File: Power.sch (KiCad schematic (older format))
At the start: 40 parts

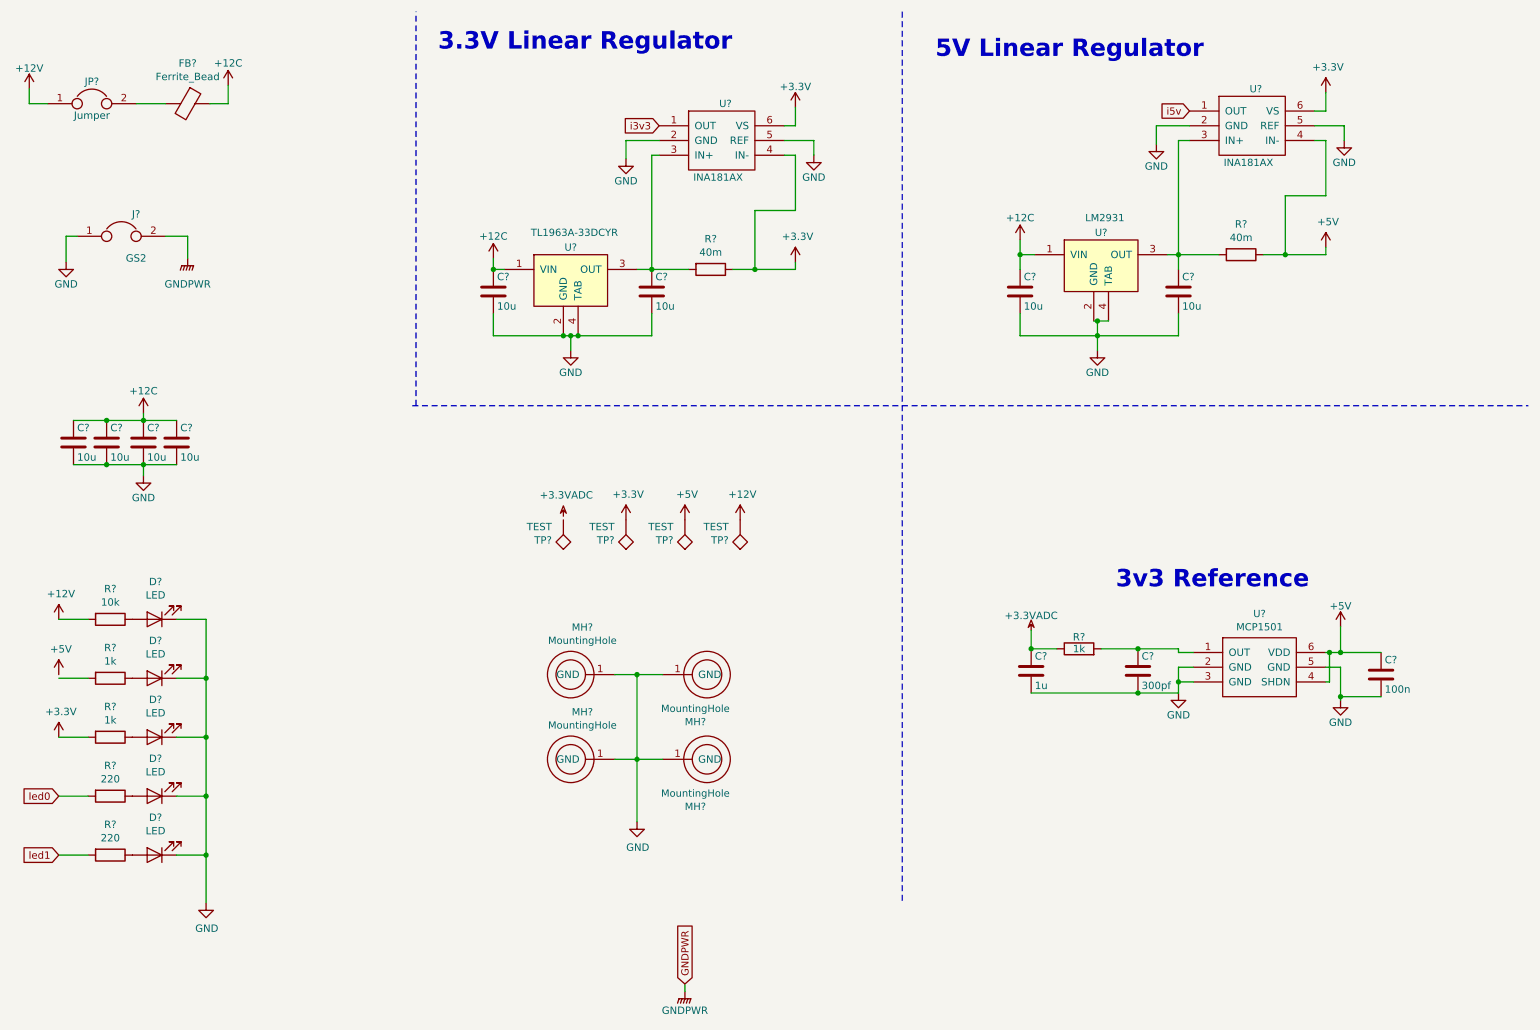
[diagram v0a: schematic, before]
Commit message: Eletrical Rules Check
Fixed some label names
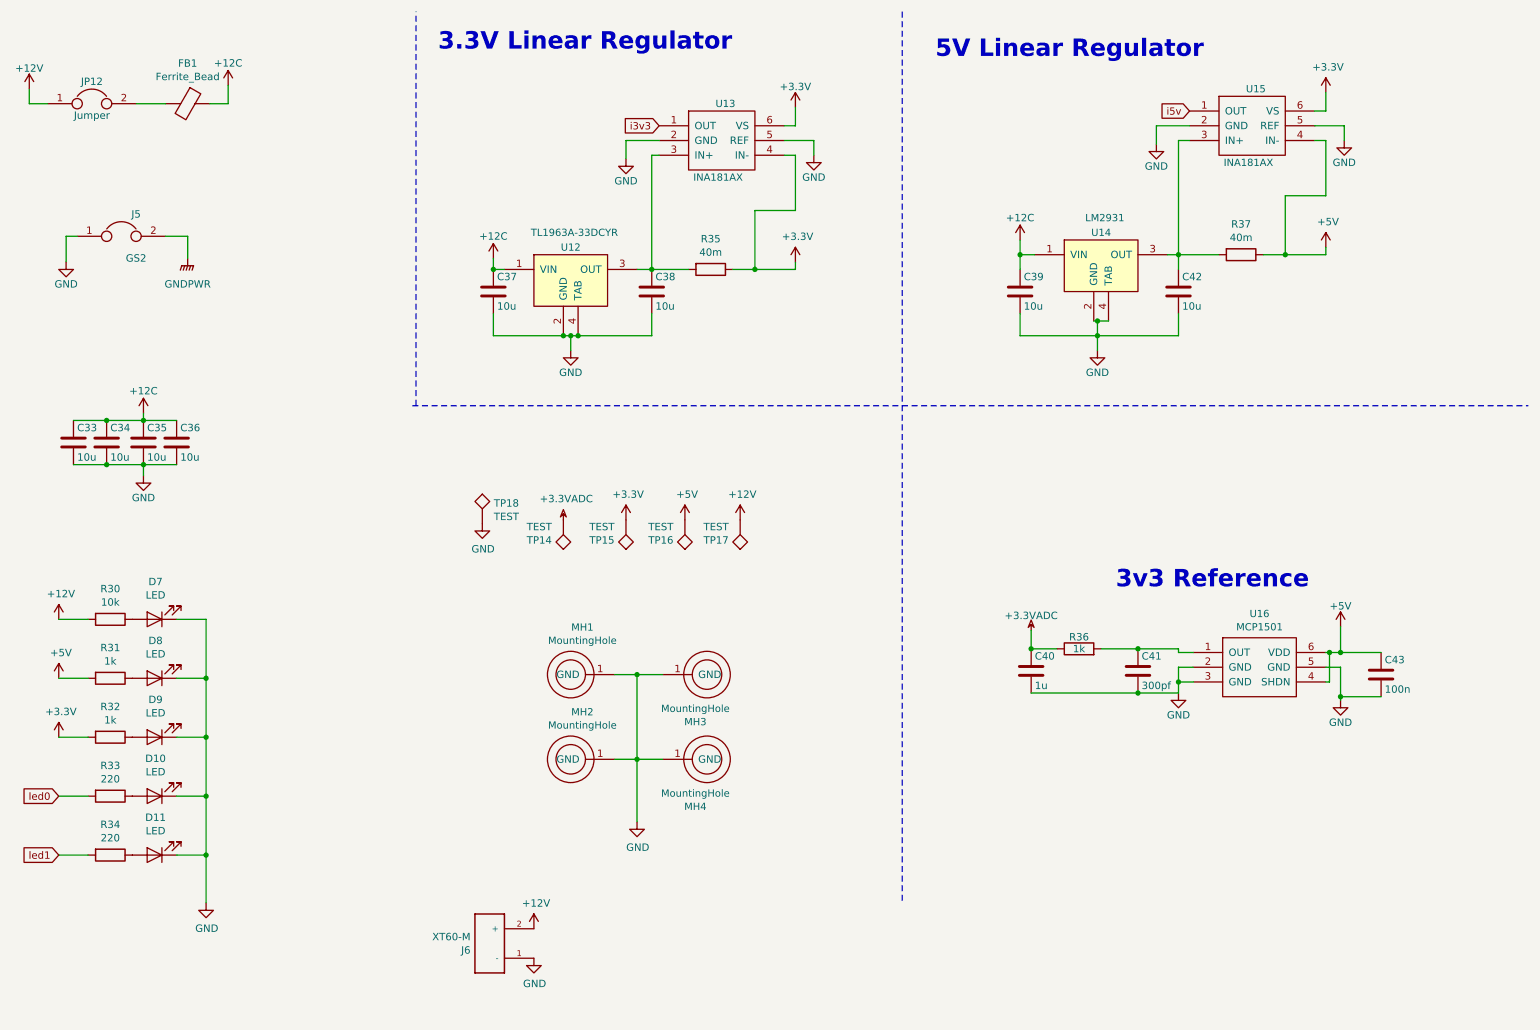
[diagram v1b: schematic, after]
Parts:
- added J6: XT60-M, AMASS_XT60-M, symbol xt60:XT60-M
- added TP18: TEST, symbol ec_2b_rescue:TEST
- gave numbers to parts that had none: 40
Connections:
- net +12V: now also J6.2 (+)
- net +3.3VADC: now also TP14.1
- net +5V: now also R31.2
- net GND: now also J6.1 (-), TP18.1

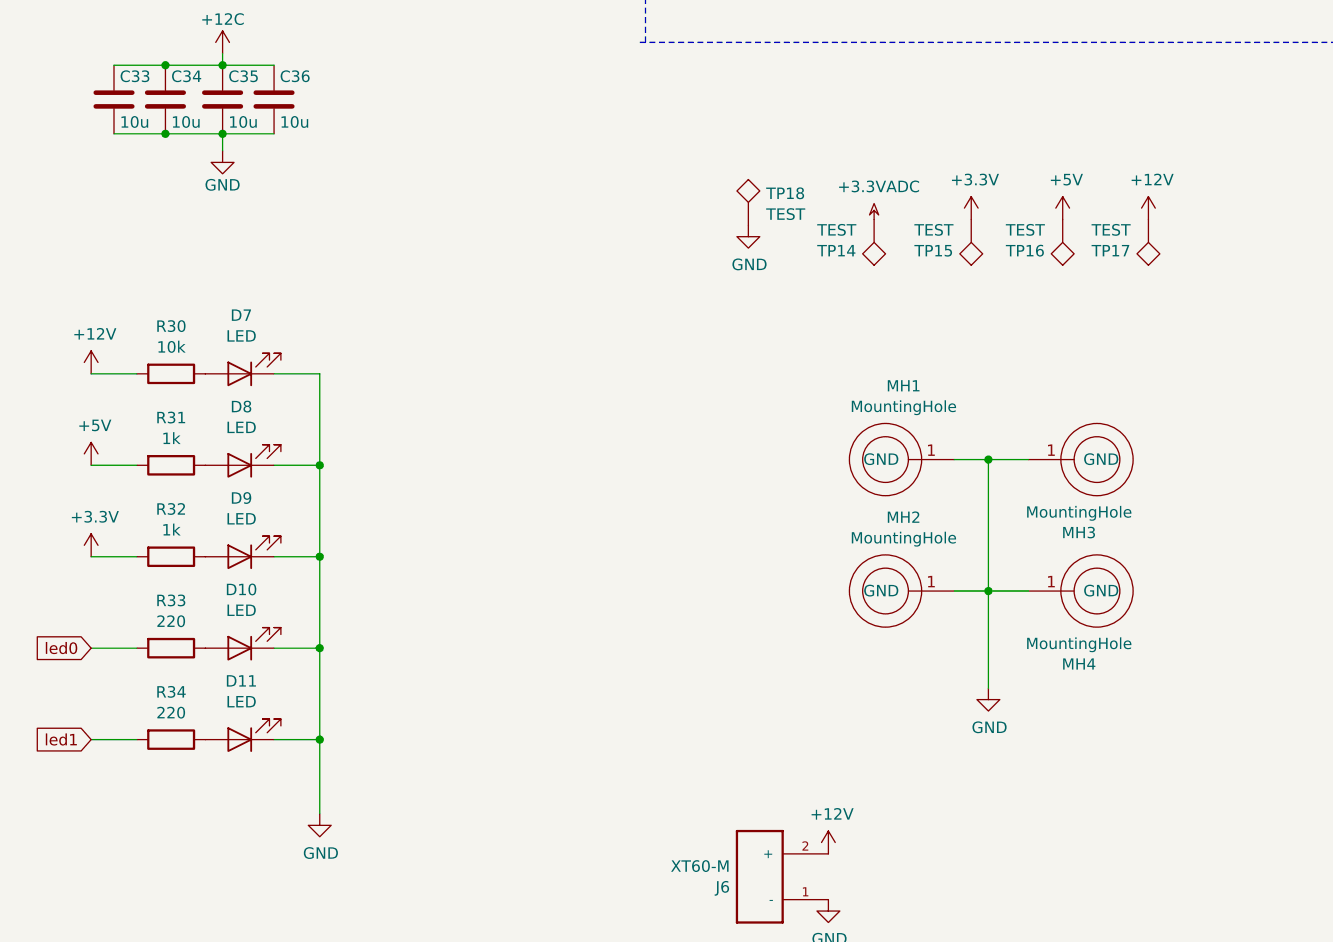
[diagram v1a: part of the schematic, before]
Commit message: Formatting Changes
Made some minor formatting changes. Documented motor channels. Fixed in labels of motor channel.
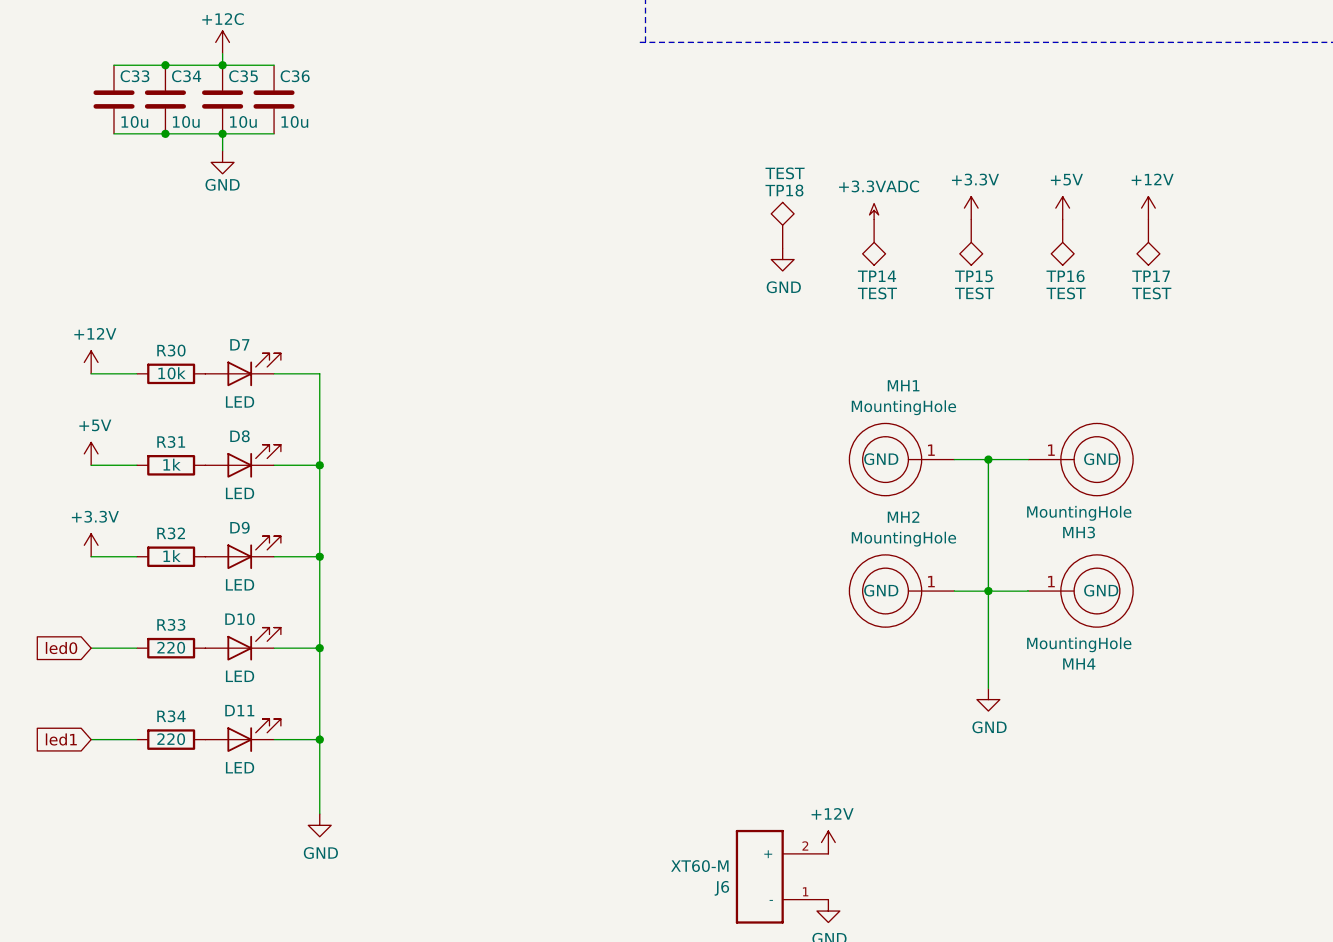
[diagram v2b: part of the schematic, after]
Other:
- moved on the sheet: TP18
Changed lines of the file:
@@
 $Descr A4 11693 8268
 encoding utf-8
-Sheet 12 12
+Sheet 9 12
 Title "Engine Controller Series 3"
 Date ""
@@
 U 1 1 5E6998D2
 P 5875 3925
-F 0 "TP17" H 5953 4063 50  0000 L CNN
-F 1 "TEST" H 5953 3972 50  0000 L CNN
+F 0 "TP17" H 5775 4175 50  0000 L CNN
+F 1 "TEST" H 5775 4250 50  0000 L CNN
 F 2 "" H 5875 3925 50  0001 C CNN
 F 3 "" H 5875 3925 50  0001 C CNN
@@
 U 1 1 5E69A32A
 P 5500 3925
-F 0 "TP16" H 5578 4063 50  0000 L CNN
-F 1 "TEST" H 5578 3972 50  0000 L CNN
+F 0 "TP16" H 5400 4175 50  0000 L CNN
+F 1 "TEST" H 5400 4250 50  0000 L CNN
 F 2 "" H 5500 3925 50  0001 C CNN
 F 3 "" H 5500 3925 50  0001 C CNN
@@
 U 1 1 5E69BC8C
 P 5100 3925
-F 0 "TP15" H 5178 4063 50  0000 L CNN
-F 1 "TEST" H 5178 3972 50  0000 L CNN
+F 0 "TP15" H 5000 4175 50  0000 L CNN
+F 1 "TEST" H 5000 4250 50  0000 L CNN
 F 2 "" H 5100 3925 50  0001 C CNN
 F 3 "" H 5100 3925 50  0001 C CNN
@@
 $EndComp
 $Comp
-L Device:LED D7
-U 1 1 5E6F3842
-P 1900 4600
-F 0 "D7" H 1893 4345 50  0000 C CNN
-F 1 "LED" H 1893 4436 50  0000 C CNN
-F 2 "" H 1900 4600 50  0001 C CNN
-F 3 "~" H 1900 4600 50  0001 C CNN
-	1    1900 4600
-	-1   0    0    1
-$EndComp
-$Comp
-L Device:LED D8
-U 1 1 5E6F68A1
-P 1900 5000
-F 0 "D8" H 1893 4745 50  0000 C CNN
-F 1 "LED" H 1893 4836 50  0000 C CNN
-F 2 "" H 1900 5000 50  0001 C CNN
-F 3 "~" H 1900 5000 50  0001 C CNN
-	1    1900 5000
-	-1   0    0    1
-$EndComp
-$Comp
-L Device:LED D9
-U 1 1 5E6F8653
-P 1900 5400
-F 0 "D9" H 1893 5145 50  0000 C CNN
-F 1 "LED" H 1893 5236 50  0000 C CNN
-F 2 "" H 1900 5400 50  0001 C CNN
-F 3 "~" H 1900 5400 50  0001 C CNN
-	1    1900 5400
-	-1   0    0    1
-$EndComp
-$Comp
-L Device:LED D10
-U 1 1 5E6FA391
-P 1900 5800
-F 0 "D10" H 1893 5545 50  0000 C CNN
-F 1 "LED" H 1893 5636 50  0000 C CNN
-F 2 "" H 1900 5800 50  0001 C CNN
-F 3 "~" H 1900 5800 50  0001 C CNN
-	1    1900 5800
-	-1   0    0    1
-$EndComp
-$Comp
 L Device:LED D11
 U 1 1 5E6FC143
 P 1900 6200
-F 0 "D11" H 1893 5945 50  0000 C CNN
-F 1 "LED" H 1893 6036 50  0000 C CNN
+F 0 "D11" H 1900 6075 50  0000 C CNN
+F 1 "LED" H 1900 6325 50  0000 C CNN
 F 2 "" H 1900 6200 50  0001 C CNN
 F 3 "~" H 1900 6200 50  0001 C CNN
@@
 U 1 1 5E65BE5F
 P 4675 3925
-F 0 "TP14" H 4753 4063 50  0000 L CNN
-F 1 "TEST" H 4753 3972 50  0000 L CNN
+F 0 "TP14" H 4575 4175 50  0000 L CNN
+F 1 "TEST" H 4575 4250 50  0000 L CNN
 F 2 "" H 4675 3925 50  0001 C CNN
 F 3 "" H 4675 3925 50  0001 C CNN
@@
 U 1 1 5E67F268
 P 1600 5000
-F 0 "R31" V 1393 5000 50  0000 C CNN
-F 1 "1k" V 1484 5000 50  0000 C CNN
+F 0 "R31" V 1500 5000 50  0000 C CNN
+F 1 "1k" V 1600 5000 50  0000 C CNN
 F 2 "" V 1530 5000 50  0001 C CNN
 F 3 "~" H 1600 5000 50  0001 C CNN
@@
 U 1 1 5E682C58
 P 1600 5400
-F 0 "R32" V 1393 5400 50  0000 C CNN
-F 1 "1k" V 1484 5400 50  0000 C CNN
+F 0 "R32" V 1500 5400 50  0000 C CNN
+F 1 "1k" V 1600 5400 50  0000 C CNN
 F 2 "" V 1530 5400 50  0001 C CNN
 F 3 "~" H 1600 5400 50  0001 C CNN
@@
 U 1 1 5E68682B
 P 1600 5800
-F 0 "R33" V 1393 5800 50  0000 C CNN
-F 1 "220" V 1484 5800 50  0000 C CNN
+F 0 "R33" V 1500 5800 50  0000 C CNN
+F 1 "220" V 1600 5800 50  0000 C CNN
 F 2 "" V 1530 5800 50  0001 C CNN
 F 3 "~" H 1600 5800 50  0001 C CNN
@@
 U 1 1 5E68A3FE
 P 1600 6200
-F 0 "R34" V 1393 6200 50  0000 C CNN
-F 1 "220" V 1484 6200 50  0000 C CNN
+F 0 "R34" V 1500 6200 50  0000 C CNN
+F 1 "220" V 1600 6200 50  0000 C CNN
 F 2 "" V 1530 6200 50  0001 C CNN
 F 3 "~" H 1600 6200 50  0001 C CNN
@@
 U 1 1 5E678387
 P 1600 4600
-F 0 "R30" V 1393 4600 50  0000 C CNN
-F 1 "10k" V 1484 4600 50  0000 C CNN
+F 0 "R30" V 1500 4600 50  0000 C CNN
+F 1 "10k" V 1600 4600 50  0000 C CNN
 F 2 "" V 1530 4600 50  0001 C CNN
 F 3 "~" H 1600 4600 50  0001 C CNN
@@
 L ec_2b_rescue:TEST TP18
 U 1 1 5E667DA6
-P 4125 3950
-F 0 "TP18" H 4203 4088 50  0000 L CNN
-F 1 "TEST" H 4203 3997 50  0000 L CNN
-F 2 "" H 4125 3950 50  0001 C CNN
-F 3 "" H 4125 3950 50  0001 C CNN
-	1    4125 3950
+P 4275 4050
+F 0 "TP18" H 4200 4300 50  0000 L CNN
+F 1 "TEST" H 4200 4375 50  0000 L CNN
+F 2 "" H 4275 4050 50  0001 C CNN
+F 3 "" H 4275 4050 50  0001 C CNN
+	1    4275 4050
 	1    0    0    -1
 $EndComp
@@
 L ec_2b_rescue:GND #PWR0104
 U 1 1 5E66C108
-P 4125 3950
-F 0 "#PWR0104" H 4125 3700 50  0001 C CNN
-F 1 "GND" H 4130 3777 50  0000 C CNN
-F 2 "" H 4125 3950 50  0001 C CNN
-F 3 "" H 4125 3950 50  0001 C CNN
-	1    4125 3950
+P 4275 4050
+F 0 "#PWR0104" H 4275 3800 50  0001 C CNN
+F 1 "GND" H 4280 3877 50  0000 C CNN
+F 2 "" H 4275 4050 50  0001 C CNN
+F 3 "" H 4275 4050 50  0001 C CNN
+	1    4275 4050
 	1    0    0    -1
 $EndComp
@@
 	1    0    0    -1
 $EndComp
+$Comp
+L Device:LED D10
+U 1 1 5E7D1BBA
+P 1900 5800
+F 0 "D10" H 1900 5675 50  0000 C CNN
+F 1 "LED" H 1900 5925 50  0000 C CNN
+F 2 "" H 1900 5800 50  0001 C CNN
+F 3 "~" H 1900 5800 50  0001 C CNN
+	1    1900 5800
+	-1   0    0    1
+$EndComp
+$Comp
+L Device:LED D9
+U 1 1 5E7D592D
+P 1900 5400
+F 0 "D9" H 1900 5275 50  0000 C CNN
+F 1 "LED" H 1900 5525 50  0000 C CNN
+F 2 "" H 1900 5400 50  0001 C CNN
+F 3 "~" H 1900 5400 50  0001 C CNN
+	1    1900 5400
+	-1   0    0    1
+$EndComp
+$Comp
+L Device:LED D8
+U 1 1 5E7D93E8
+P 1900 5000
+F 0 "D8" H 1900 4875 50  0000 C CNN
+F 1 "LED" H 1900 5125 50  0000 C CNN
+F 2 "" H 1900 5000 50  0001 C CNN
+F 3 "~" H 1900 5000 50  0001 C CNN
+	1    1900 5000
+	-1   0    0    1
+$EndComp
+$Comp
+L Device:LED D7
+U 1 1 5E7E0D31
+P 1900 4600
+F 0 "D7" H 1900 4475 50  0000 C CNN
+F 1 "LED" H 1900 4725 50  0000 C CNN
+F 2 "" H 1900 4600 50  0001 C CNN
+F 3 "~" H 1900 4600 50  0001 C CNN
+	1    1900 4600
+	-1   0    0    1
+$EndComp
 $EndSCHEMATC
